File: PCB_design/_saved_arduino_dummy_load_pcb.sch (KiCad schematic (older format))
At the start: 104 parts, among them J1 Barrel_Jack, J2 Conn_02x08_Counter_Clockwise, M1 REG, U1 LM324, U2 LM324

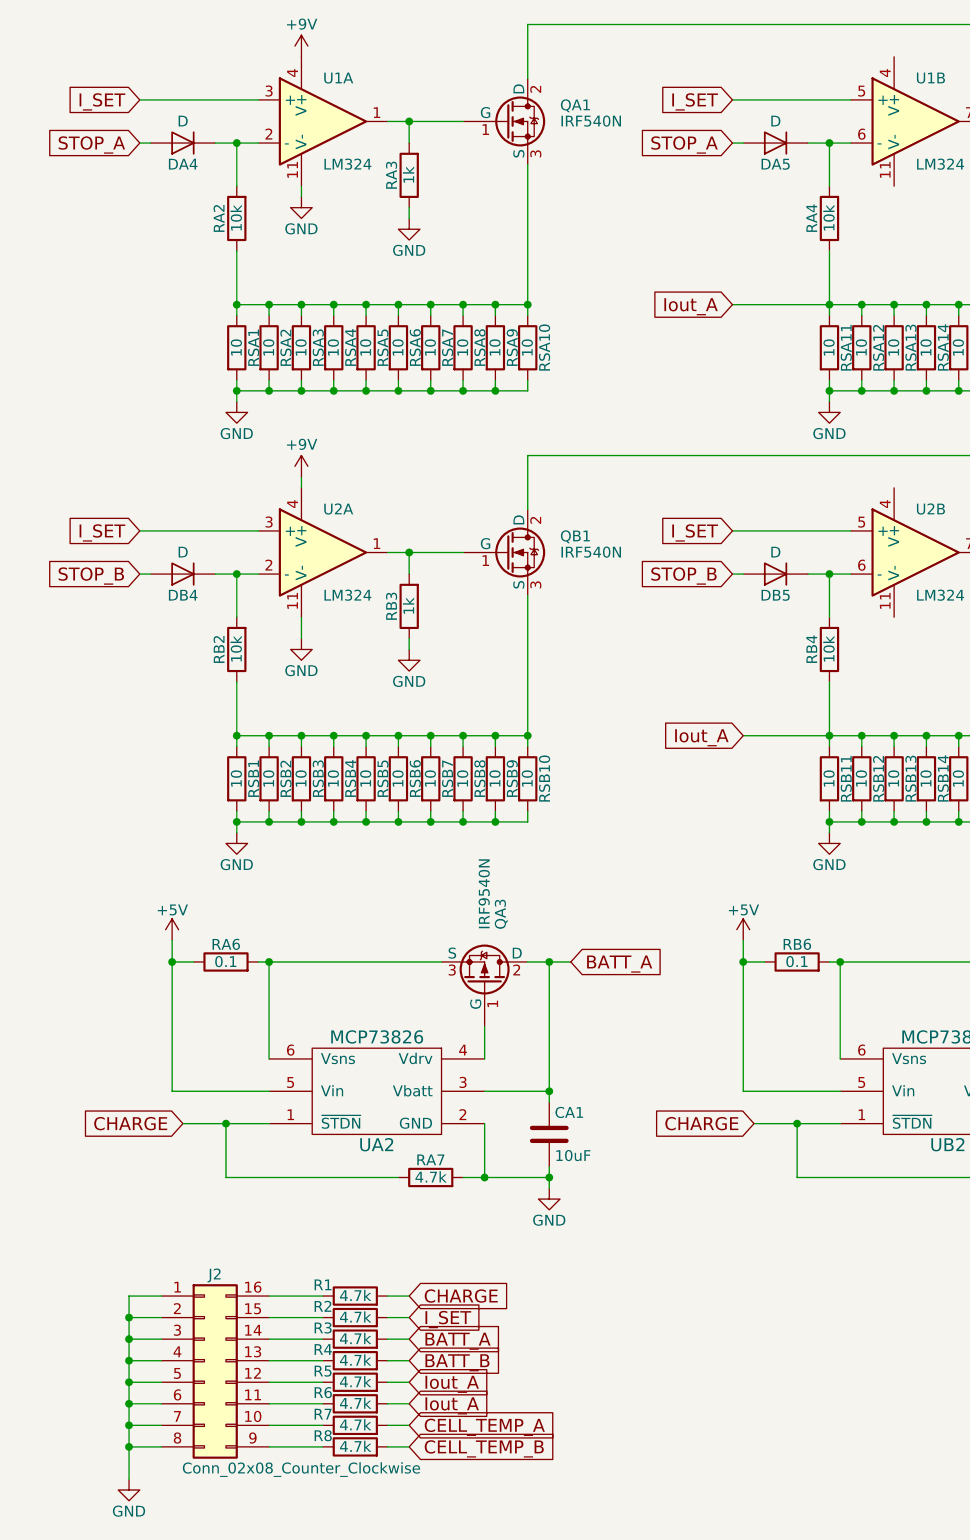
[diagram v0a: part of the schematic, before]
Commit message: Gave components footprints and started PCB layout
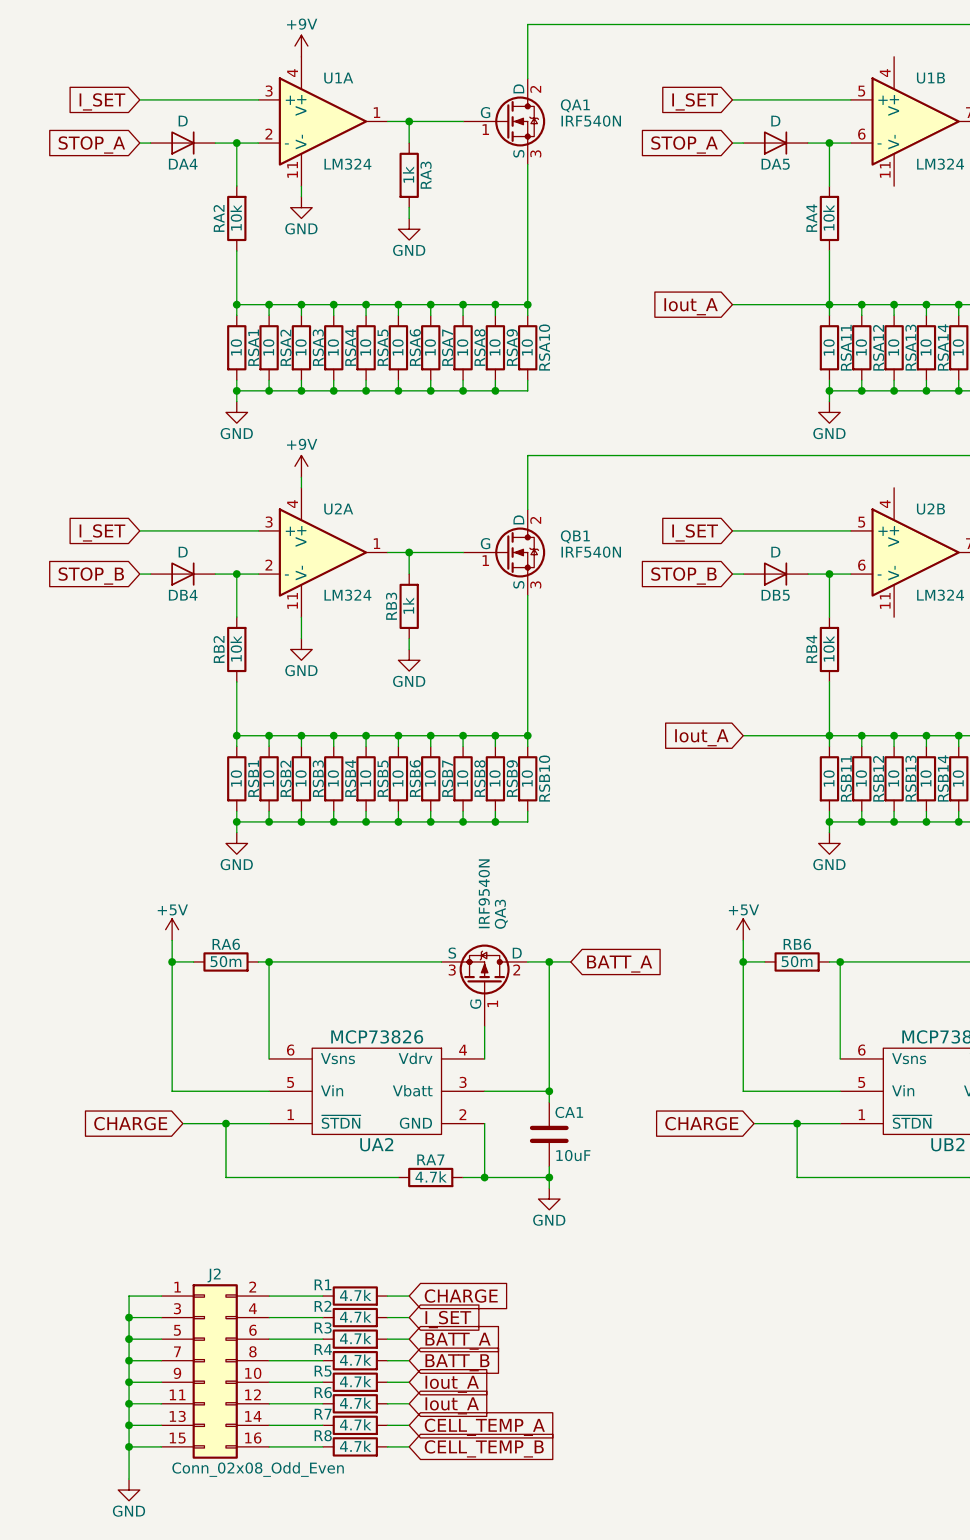
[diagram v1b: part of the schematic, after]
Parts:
- removed J2: Conn_02x08_Counter_Clockwise, symbol Conn_02x08_Counter_Clockwise
- added J2: Conn_02x08_Odd_Even, symbol Conn_02x08_Odd_Even
- C1, CA1, CA2, CA3, CB1, CB2, CB3: footprint (none) -> Capacitors_SMD:C_0805_HandSoldering
- DA1, DA2, DA3, DA4, DA5, DB1, DB2, DB3, DB4, DB5: footprint (none) -> Diodes_SMD:D_SOD-123
- J1: footprint (none) -> Connectors:JACK_ALIM
- QA1, QA2, QA3, QB1, QB2, QB3: footprint TO_SOT_Packages_THT:TO-220_Vertical -> TO_SOT_Packages_THT:TO-220-3_Vertical
- R1, R2, R3, R4, R5, R6, R7, R8, RA1, RA2, RA3, RA4, RA5, RA7, RB1, RB2, RB3, RB4, RB5, RB7: footprint (none) -> Resistors_SMD:R_0805_HandSoldering
- RA6, RB6: value 0.1 -> 50m; footprint (none) -> Resistors_SMD:R_2512_HandSoldering
- RSA1, RSA10, RSA11, RSA12, RSA13, RSA14, RSA15, RSA16, RSA17, RSA18, RSA19, RSA2, RSA20, RSA3, RSA4, RSA5, RSA6, RSA7, RSA8, RSA9, RSB1, RSB10, RSB11, RSB12, RSB13, RSB14, RSB15, RSB16, RSB17, RSB18, RSB19, RSB2, RSB20, RSB3, RSB4, RSB5, RSB6, RSB7, RSB8, RSB9: footprint (none) -> Resistors_THT:R_Axial_DIN0617_L17.0mm_D6.0mm_P7.62mm_Vertical
- RVA1, RVA2, RVB1, RVB2: footprint (none) -> Potentiometers:Potentiometer_Trimmer_ACP_CA6v_Horizontal_MountLS
- TA1, TA2, TA3, TB1, TB2, TB3: footprint (none) -> TO_SOT_Packages_THT:TO-92_Inline_Wide
- U1, U2: footprint (none) -> Housings_SOIC:SOIC-14_3.9x8.7mm_Pitch1.27mm
- UA2, UB2: footprint (none) -> TO_SOT_Packages_SMD:SOT-23-6_Handsoldering
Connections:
- net GND: now also RA3.2, J2.1 (Pin_1), J2.11 (Pin_11), J2.13 (Pin_13), J2.15 (Pin_15), J2.3 (Pin_3), J2.5 (Pin_5), J2.7 (Pin_7), J2.9 (Pin_9); no longer RA3.1
- net at QA1.1 (G), U1.1: now also RA3.1; no longer RA3.2
- net at R1.1: now also J2.2 (Pin_2)
- net at R2.1: now also J2.4 (Pin_4)
- net at R7.1: now also J2.14 (Pin_14)
- net at R6.1: now also J2.12 (Pin_12)
- net at R5.1: now also J2.10 (Pin_10)
- net at R4.1: now also J2.8 (Pin_8)
- net at R3.1: now also J2.6 (Pin_6)
- net at R8.1: now also J2.16 (Pin_16)
